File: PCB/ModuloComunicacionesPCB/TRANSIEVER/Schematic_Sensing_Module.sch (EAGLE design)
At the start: 73 parts, among them Q1 CSM-7X-DU, T1 TERMINAL-TB3, T2 TERMINAL-TB3, T3 TERMINAL-TB3

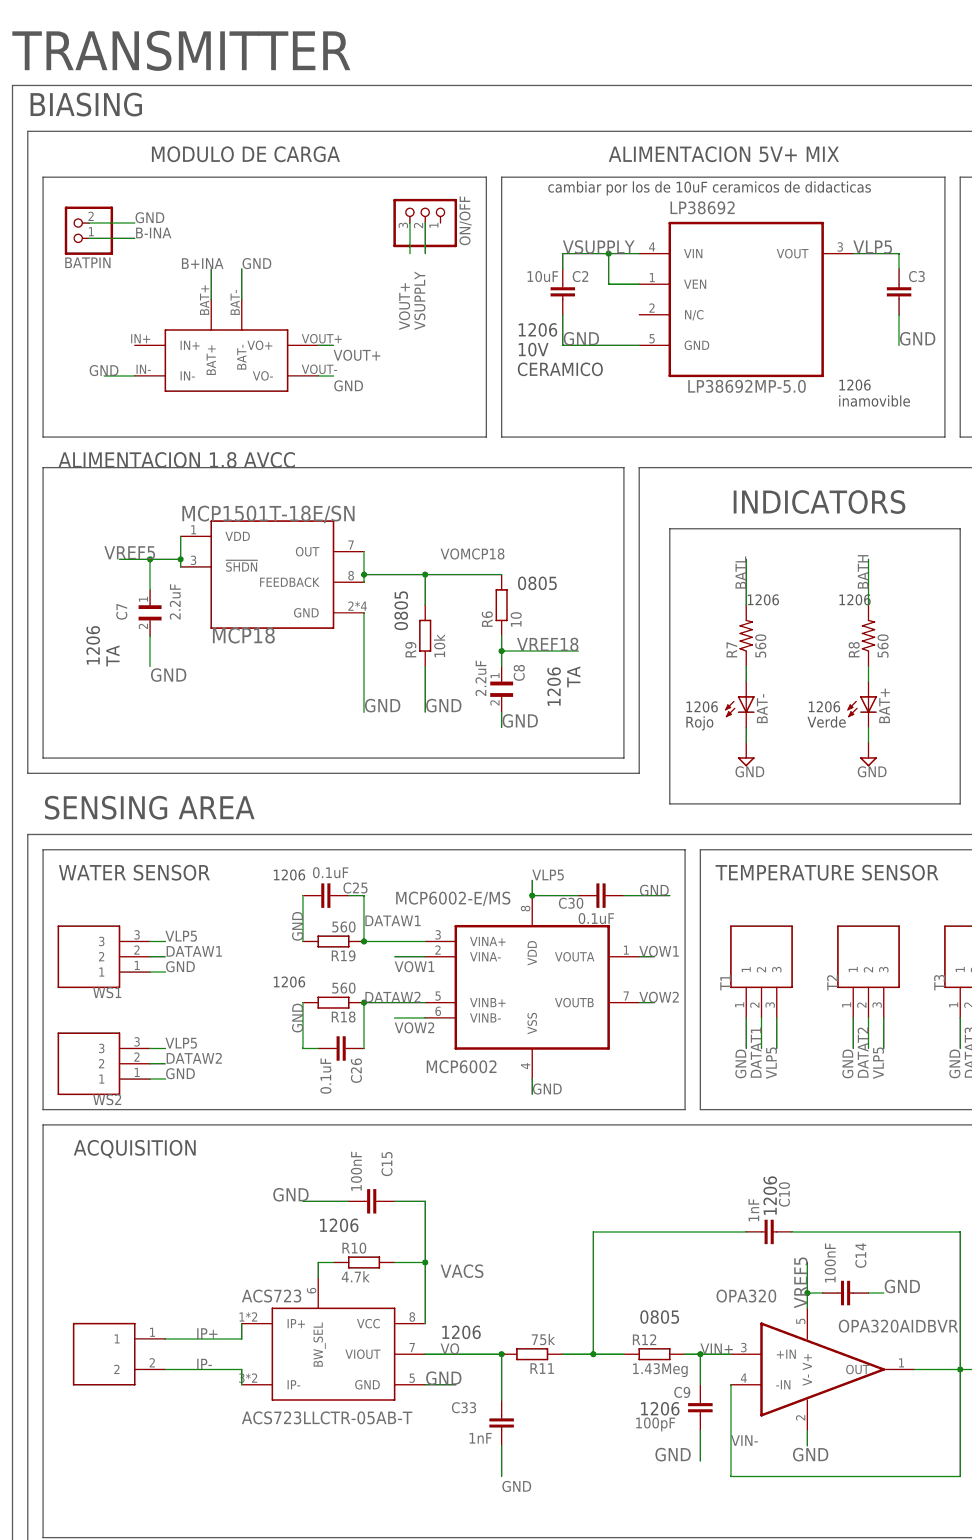
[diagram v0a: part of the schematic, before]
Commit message: pcb enviadas a produccion
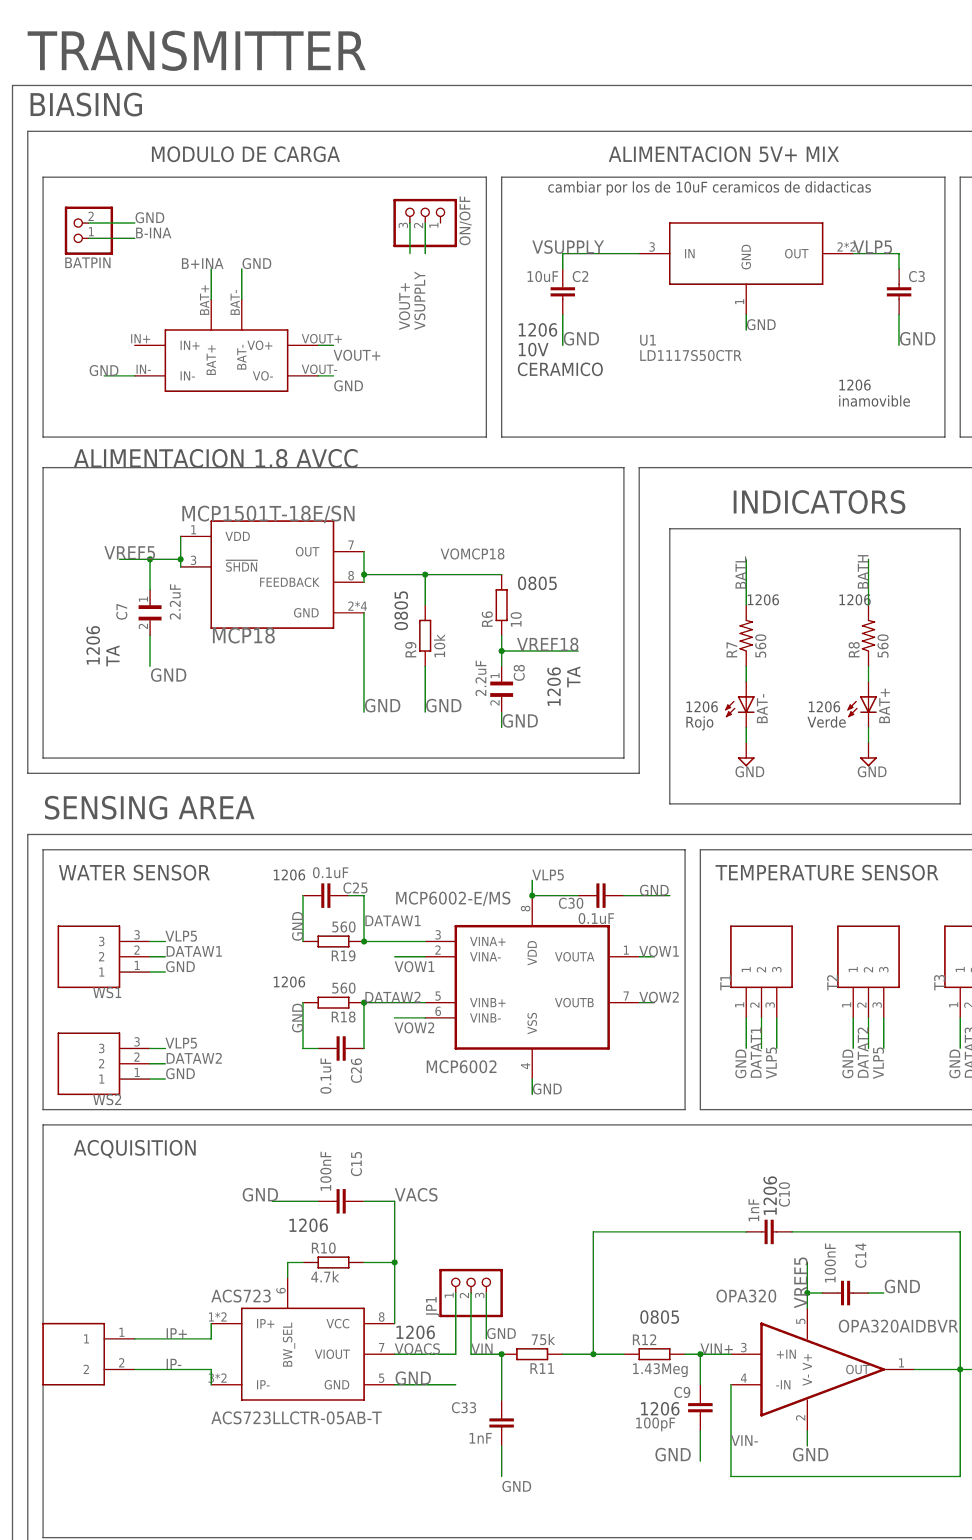
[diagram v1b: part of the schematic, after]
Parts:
- removed LP38692: LP38692MP-5.0, LP38692MP-5.0:LP38692MP-5.0
- added JP1: (no value), pinhead:PINHD-1X3
- added U1: LD1117S50CTR, LD1117S50CTR:LD1117S50CTR
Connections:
- removed net VO: ACS723.VIOUT, C33.1, R11.2
- new net VIN: C33.1, JP1.2, R11.2
- new net VOACS: ACS723.VIOUT, JP1.1
- net GND: now also JP1.3, U1.GND; no longer LP38692.GND
- net VLP5: now also U1.OUT; no longer LP38692.VOUT
- net VSUPPLY: now also U1.IN; no longer LP38692.VEN, LP38692.VIN
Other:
- moved on the sheet: ACS723, C15, R10
